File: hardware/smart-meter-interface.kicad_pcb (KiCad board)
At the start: 2 copper layers, 32 x 32 mm, 36 parts, among them J1 USB_B_Micro, Q3 SFH309, Q4 BC817W, Q5 BC807W, U1 CH340X, U2 ESP32-WROOM-32, U4 74LVC1G17, U5 74LVC1G17

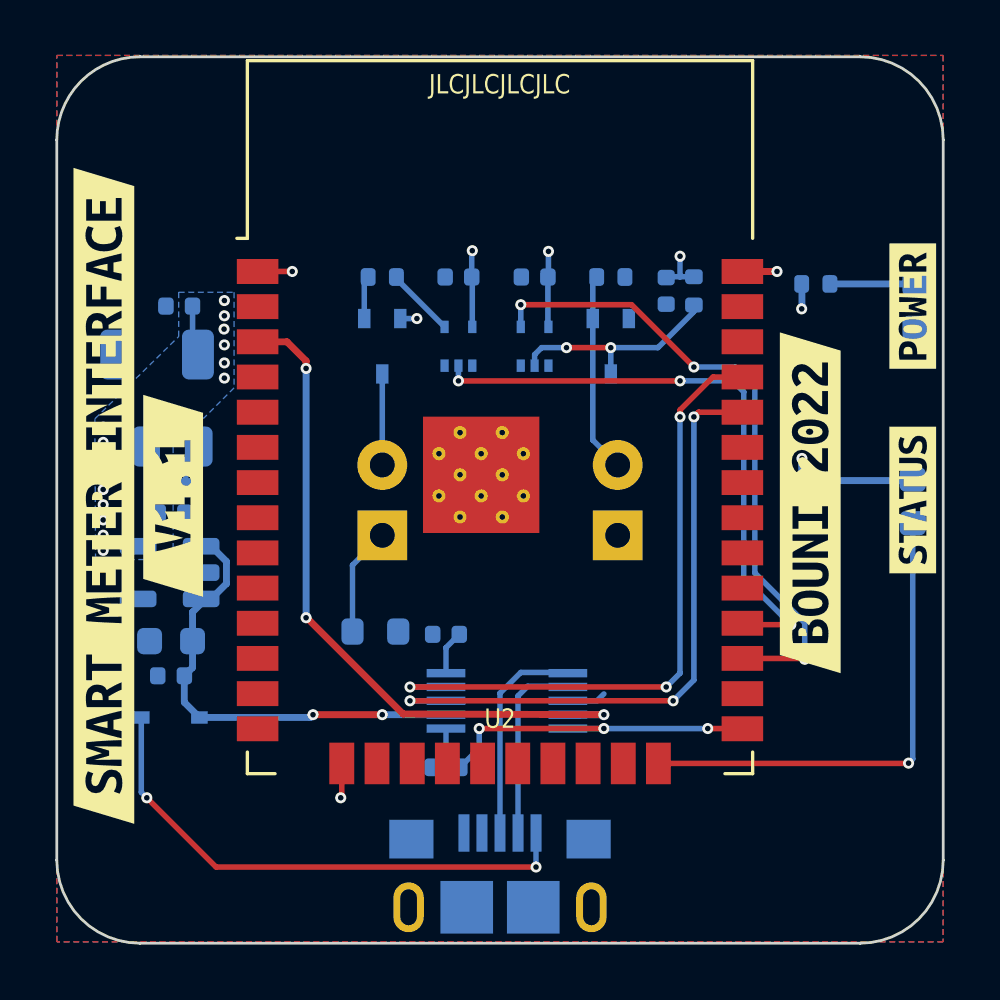
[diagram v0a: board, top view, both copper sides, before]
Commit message: shrinked pcb further to 28x28mm
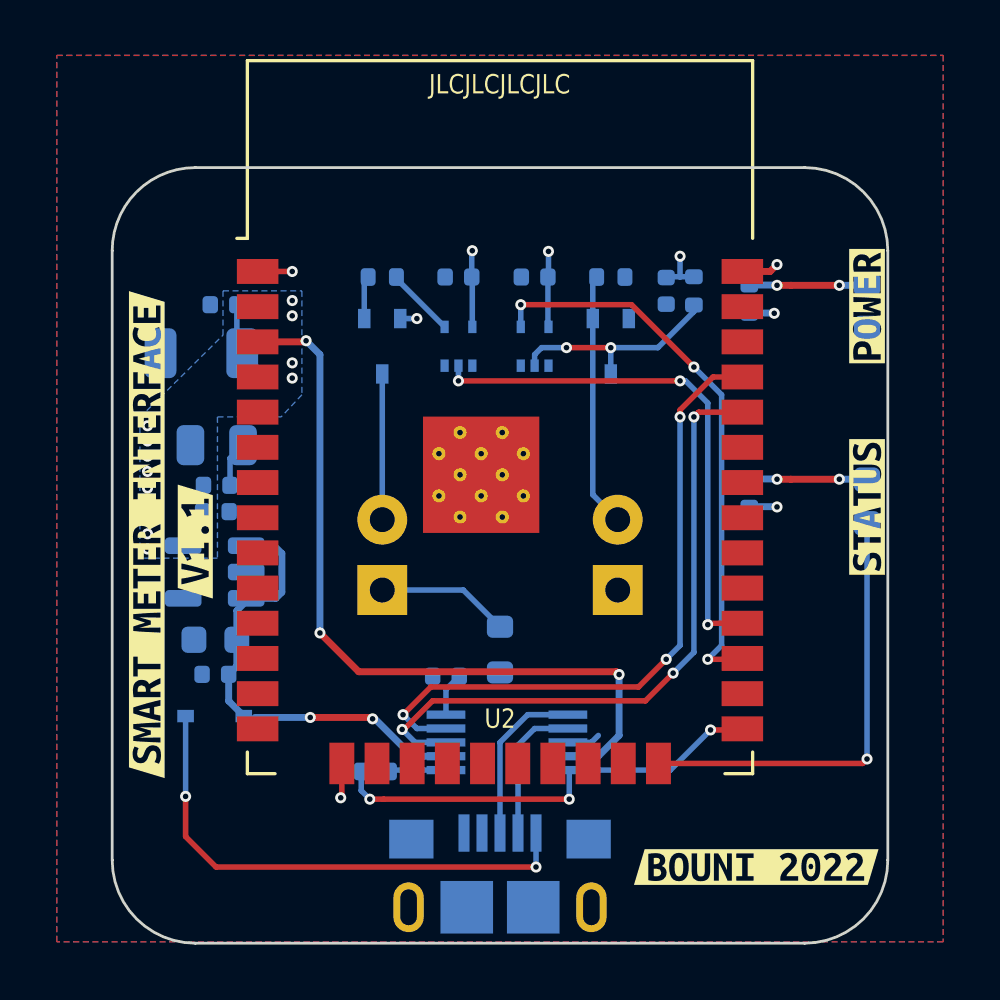
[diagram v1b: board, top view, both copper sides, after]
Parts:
- removed kibuzzard-635BBB2F: G***, kibuzzard-635BBB2F
- removed kibuzzard-635BBB3D: G***, kibuzzard-635BBB3D
- removed kibuzzard-651E6B99: G***, kibuzzard-651E6B99
- removed kibuzzard-651E6BC2: G***, kibuzzard-651E6BC2
- removed kibuzzard-651E6BCC: G***, kibuzzard-651E6BCC
- added kibuzzard-651E74C0: G***, kibuzzard-651E74C0, F.Cu at (45.0, 57.5)
- added kibuzzard-651E74D1: G***, kibuzzard-651E74D1, F.Cu at (43.2, 57.2)
- added kibuzzard-651E74E3: G***, kibuzzard-651E74E3, F.Cu at (65.2, 69.2)
- added kibuzzard-651E74F7: G***, kibuzzard-651E74F7, F.Cu at (69.2, 56.2)
- added kibuzzard-651E7500: G***, kibuzzard-651E7500, F.Cu at (69.2, 49.0)
- moved R7 4.55 mm to (56.0, 61.4), turned to -90 degrees
- moved R12 2.55 mm to (51.5, 65.8), turned to 180 degrees
- moved R8 2.46 mm to (65.0, 48.8), turned to 90 degrees
- moved R9 2.44 mm to (65.0, 55.8), turned to 90 degrees
- moved D5 1.98 mm to (51.8, 59.2)
- moved Q3 1.98 mm to (60.2, 59.2)
- moved D3 1.75 mm to (69.2, 49.0)
- moved D4 1.65 mm to (69.2, 56.0)
- moved LDO1 1.63 mm to (45.7, 58.6)
- moved C5 1.60 mm to (45.8, 55.5)
- moved D2 1.60 mm to (45.7, 63.8)
- moved C2 1.60 mm to (45.7, 62.3)
- moved C3 1.60 mm to (45.7, 61.0)
- moved C6 1.60 mm to (45.8, 54.0)
- moved C7 1.60 mm to (45.2, 50.7)
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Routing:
- net IO0: track 12.5 -> 16.3 mm
- net EN: track 24.8 -> 28.4 mm
- net RX: track 23.3 -> 20.4 mm
- net BLINK: track 21.7 -> 19.0 mm
- net Net-(D5-A): track 3.28 -> 5.26 mm
- net Net-(Q3-E): track 7.22 -> 9.19 mm
- net IO2: track 17.9 -> 16.1 mm
- net /D+: track 7.81 -> 6.14 mm
- net /D-: track 6.89 -> 5.22 mm
- net Net-(D4-A): track 3.05 -> 4.29 mm, vias 0 -> 2
- net Net-(D3-A): track 3.30 -> 4.34 mm, vias 0 -> 2
- net Net-(D5-K): track 3.92 -> 4.80 mm
- net Net-(D2-A): track 19.3 -> 18.7 mm
- net RXD0: track 23.2 -> 23.8 mm
- net TXD0: track 23.5 -> 24.0 mm
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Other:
- board size 32 x 32 mm -> 28 x 28 mm

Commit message: Minor improvements
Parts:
- removed kibuzzard-651E74C0: G***, kibuzzard-651E74C0
- removed kibuzzard-651E74D1: G***, kibuzzard-651E74D1
- removed kibuzzard-651E74E3: G***, kibuzzard-651E74E3
- added kibuzzard-651FCF74: G***, kibuzzard-651FCF74, F.Cu at (56.0, 67.8)
- added kibuzzard-651FCFB8: G***, kibuzzard-651FCFB8, F.Cu at (65.3, 69.3)
- added kibuzzard-651FCFC3: G***, kibuzzard-651FCFC3, F.Cu at (46.8, 69.3)
- moved R9 5.36 mm to (65.2, 50.4), turned to -90 degrees
- moved C1 2.81 mm to (51.5, 63.5)
- moved R7 0.70 mm to (56.2, 62.0), turned to 0 degrees
- moved R6 0.50 mm to (63.5, 48.5)
- moved R8 0.39 mm to (65.2, 48.5)
- moved R12 0.20 mm to (51.5, 66.0)
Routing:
- net TXD0: track 24.0 -> 30.1 mm
- net RXD0: track 23.8 -> 29.8 mm
- net Net-(D4-A): track 4.29 -> 7.91 mm
- net +5V: track 16.9 -> 18.1 mm
- net Net-(U1-V3): track 1.60 -> 2.16 mm
- net +3V3: track 11.4 -> 11.6 mm, vias 19 -> 18

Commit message: Minor improvements
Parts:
- added TH: ToolingHole, JLCPCB:ToolingHole, F.Cu at (45.5, 71.0)
- added TH: ToolingHole, JLCPCB:ToolingHole, F.Cu at (66.5, 71.0)
- added TH: ToolingHole, JLCPCB:ToolingHole, F.Cu at (45.5, 45.0)
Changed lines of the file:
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@@
     (property ki_fp_filters "ESP32?WROOM?32*")
     (sheetfile "smart-meter-interface.kicad_sch")
-    (attr smd exclude_from_pos_files dnp)
+    (attr smd exclude_from_pos_files exclude_from_bom dnp)
     (fp_line (start -9.12 -15.86) (end -9.12 -9.445)
       (stroke (width 0.12) (type solid)) (layer "F.SilkS"))
@@
       (stroke (width 0) (type solid)) (fill solid) (layer "F.SilkS"))
   )
+  (footprint "JLCPCB:ToolingHole" (layer "F.Cu")
+    (at 45.5 71)
+    (property "Reference" "TH" (at 0 -4.27 0 unlocked) (layer "F.SilkS") hide
+      (effects (font (size 1 1) (thickness 0.15)))
+    )
+    (property "Value" "ToolingHole" (at 0 -2.77 0 unlocked) (layer "F.Fab") hide
+      (effects (font (size 1 1) (thickness 0.15)))
+    )
+    (property "Footprint" "JLCPCB:ToolingHole" (at 0 0 0 unlocked) (layer "F.Fab") hide
+      (effects (font (size 1.27 1.27)))
+    )
+    (property "Datasheet" "" (at 0 0 0 unlocked) (layer "F.Fab") hide
+      (effects (font (size 1.27 1.27)))
+    )
+    (property "Description" "" (at 0 0 0 unlocked) (layer "F.Fab") hide
+      (effects (font (size 1.27 1.27)))
+    )
+    (attr board_only exclude_from_pos_files exclude_from_bom allow_missing_courtyard dnp)
+    (fp_text user "${REFERENCE}" (at 0 -1.27 0 unlocked) (layer "F.Fab") hide
+      (effects (font (size 1 1) (thickness 0.15)))
+    )
+    (pad "" np_thru_hole circle (at 0 0) (size 1.4 1.4) (drill 1.152) (layers "*.Mask")
+    )
+  )
   (footprint "kibuzzard-651E7500" (layer "F.Cu")
     (at 69.25 49 90)
@@
       (stroke (width 0) (type solid)) (fill solid) (layer "F.SilkS"))
   )
+  (footprint "JLCPCB:ToolingHole" (layer "F.Cu")
+    (at 66.5 71)
+    (property "Reference" "TH" (at 0 -4.27 0 unlocked) (layer "F.SilkS") hide
+      (effects (font (size 1 1) (thickness 0.15)))
+    )
+    (property "Value" "ToolingHole" (at 0 -2.77 0 unlocked) (layer "F.Fab") hide
+      (effects (font (size 1 1) (thickness 0.15)))
+    )
+    (property "Footprint" "JLCPCB:ToolingHole" (at 0 0 0 unlocked) (layer "F.Fab") hide
+      (effects (font (size 1.27 1.27)))
+    )
+    (property "Datasheet" "" (at 0 0 0 unlocked) (layer "F.Fab") hide
+      (effects (font (size 1.27 1.27)))
+    )
+    (property "Description" "" (at 0 0 0 unlocked) (layer "F.Fab") hide
+      (effects (font (size 1.27 1.27)))
+    )
+    (attr board_only exclude_from_pos_files exclude_from_bom allow_missing_courtyard dnp)
+    (fp_text user "${REFERENCE}" (at 0 -1.27 0 unlocked) (layer "F.Fab") hide
+      (effects (font (size 1 1) (thickness 0.15)))
+    )
+    (pad "" np_thru_hole circle (at 0 0) (size 1.4 1.4) (drill 1.152) (layers "*.Mask")
+    )
+  )
   (footprint "kibuzzard-651FCFC3" (layer "F.Cu")
     (at 46.75 69.35)
@@
       (stroke (width 0) (type solid)) (fill solid) (layer "F.SilkS"))
   )
+  (footprint "JLCPCB:ToolingHole" (layer "F.Cu")
+    (at 45.5 45)
+    (property "Reference" "TH" (at 0 -4.27 0 unlocked) (layer "F.SilkS") hide
+      (effects (font (size 1 1) (thickness 0.15)))
+    )
+    (property "Value" "ToolingHole" (at 0 -2.77 0 unlocked) (layer "F.Fab") hide
+      (effects (font (size 1 1) (thickness 0.15)))
+    )
+    (property "Footprint" "JLCPCB:ToolingHole" (at 0 0 0 unlocked) (layer "F.Fab") hide
+      (effects (font (size 1.27 1.27)))
+    )
+    (property "Datasheet" "" (at 0 0 0 unlocked) (layer "F.Fab") hide
+      (effects (font (size 1.27 1.27)))
+    )
+    (property "Description" "" (at 0 0 0 unlocked) (layer "F.Fab") hide
+      (effects (font (size 1.27 1.27)))
+    )
+    (attr board_only exclude_from_pos_files exclude_from_bom allow_missing_courtyard dnp)
+    (fp_text user "${REFERENCE}" (at 0 -1.27 0 unlocked) (layer "F.Fab") hide
+      (effects (font (size 1 1) (thickness 0.15)))
+    )
+    (pad "" np_thru_hole circle (at 0 0) (size 1.4 1.4) (drill 1.152) (layers "*.Mask")
+    )
+  )
   (footprint "kibuzzard-651FCFB8" (layer "F.Cu")
     (at 65.35 69.35)
@@
     (property ki_fp_filters "LED*3.0mm*Clear*")
     (sheetfile "smart-meter-interface.kicad_sch")
-    (attr through_hole dnp)
+    (attr through_hole exclude_from_pos_files exclude_from_bom dnp)
     (fp_line (start -0.29 -1.236) (end -0.29 -1.08)
       (stroke (width 0.12) (type solid)) (layer "B.SilkS"))
@@
     (property ki_fp_filters "LED*3.0mm*IRBlack*")
     (sheetfile "smart-meter-interface.kicad_sch")
-    (attr through_hole dnp)
+    (attr through_hole exclude_from_pos_files exclude_from_bom dnp)
     (fp_line (start -0.29 -1.236) (end -0.29 -1.08)
       (stroke (width 0.12) (type solid)) (layer "B.SilkS"))
@@
     (effects (font (size 0.7 0.6) (thickness 0.1)) (justify mirror))
   )
-  (gr_text "JLCJLCJLCJLC" (at 55.986 41 0) (layer "F.SilkS")
+  (gr_text "JLCJLCJLCJLC" (at 55.986 45 0) (layer "F.SilkS")
     (effects (font (size 0.7 0.6) (thickness 0.1)))
   )

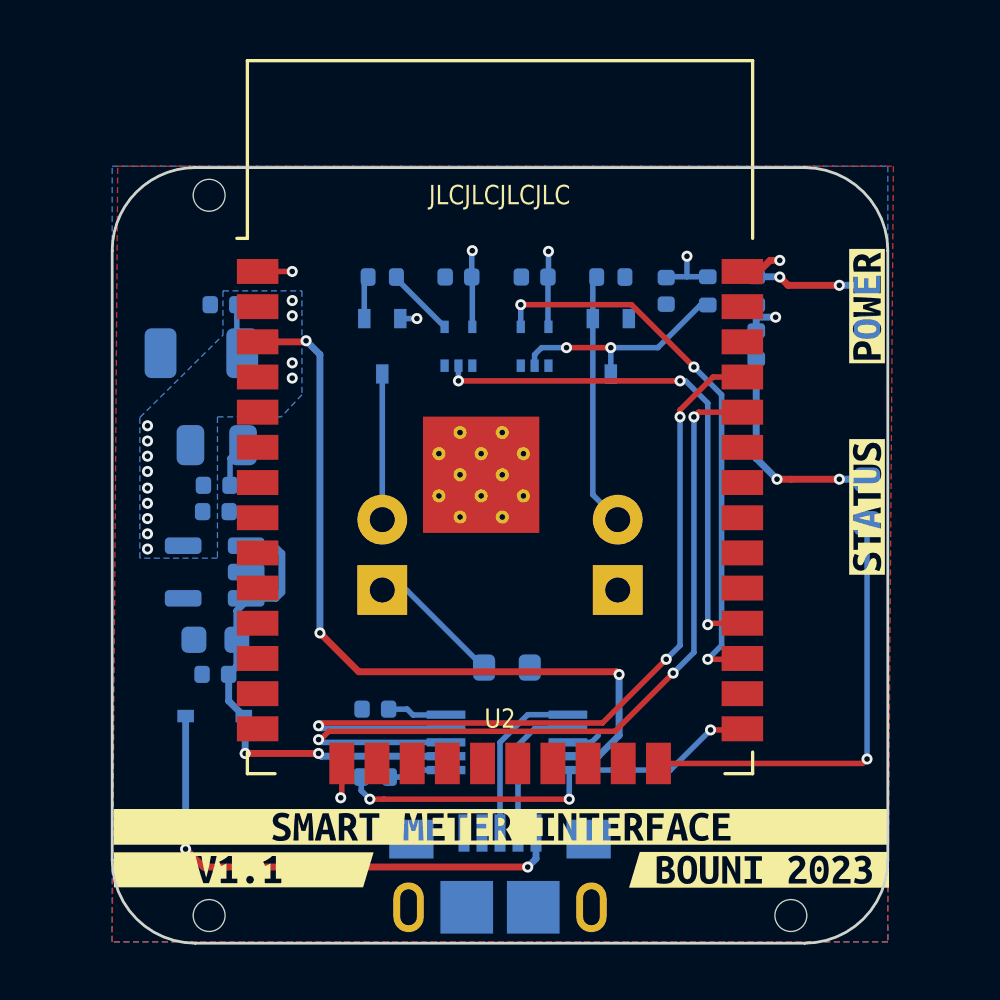
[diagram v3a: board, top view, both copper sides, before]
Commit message: Streamlined annotations
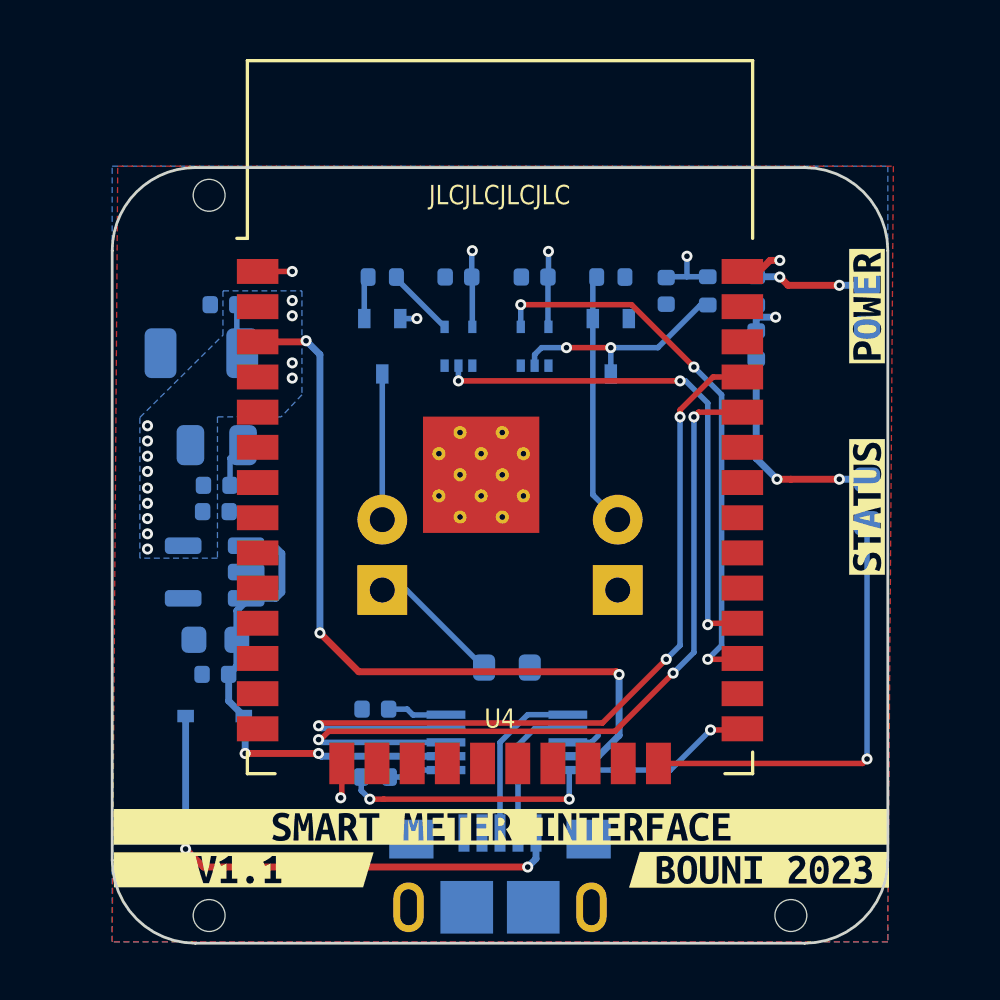
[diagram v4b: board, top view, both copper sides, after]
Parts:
- renumbered C9 to C1, C7 to C10, C8 to C11, C10 to C2, C11 to C3, C1 to C4, C2 to C5, C3 to C6, C4 to C7, C5 to C8, C6 to C9, D5 to D1, Q3 to Q1, Q4 to Q2, Q5 to Q3, R3 to R1, R6 to R2, R7 to R3, R2 to R4, R12 to R5, R8 to R6, R9 to R7, U4 to U1, U5 to U2, U1 to U3, U2 to U4
